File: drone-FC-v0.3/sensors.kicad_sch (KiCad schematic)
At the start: 34 parts, among them J2 Conn_01x04_Pin, J6 Conn_01x04_Pin, J7 ICM, J8 UART0, U3 LSM6DSOX, U4 MS5607-02BA, U5 LIS3MDL, U6 LIS3MDL, U7 MS5607-02BA, U8 LSM6DSOX, U9 BMI088

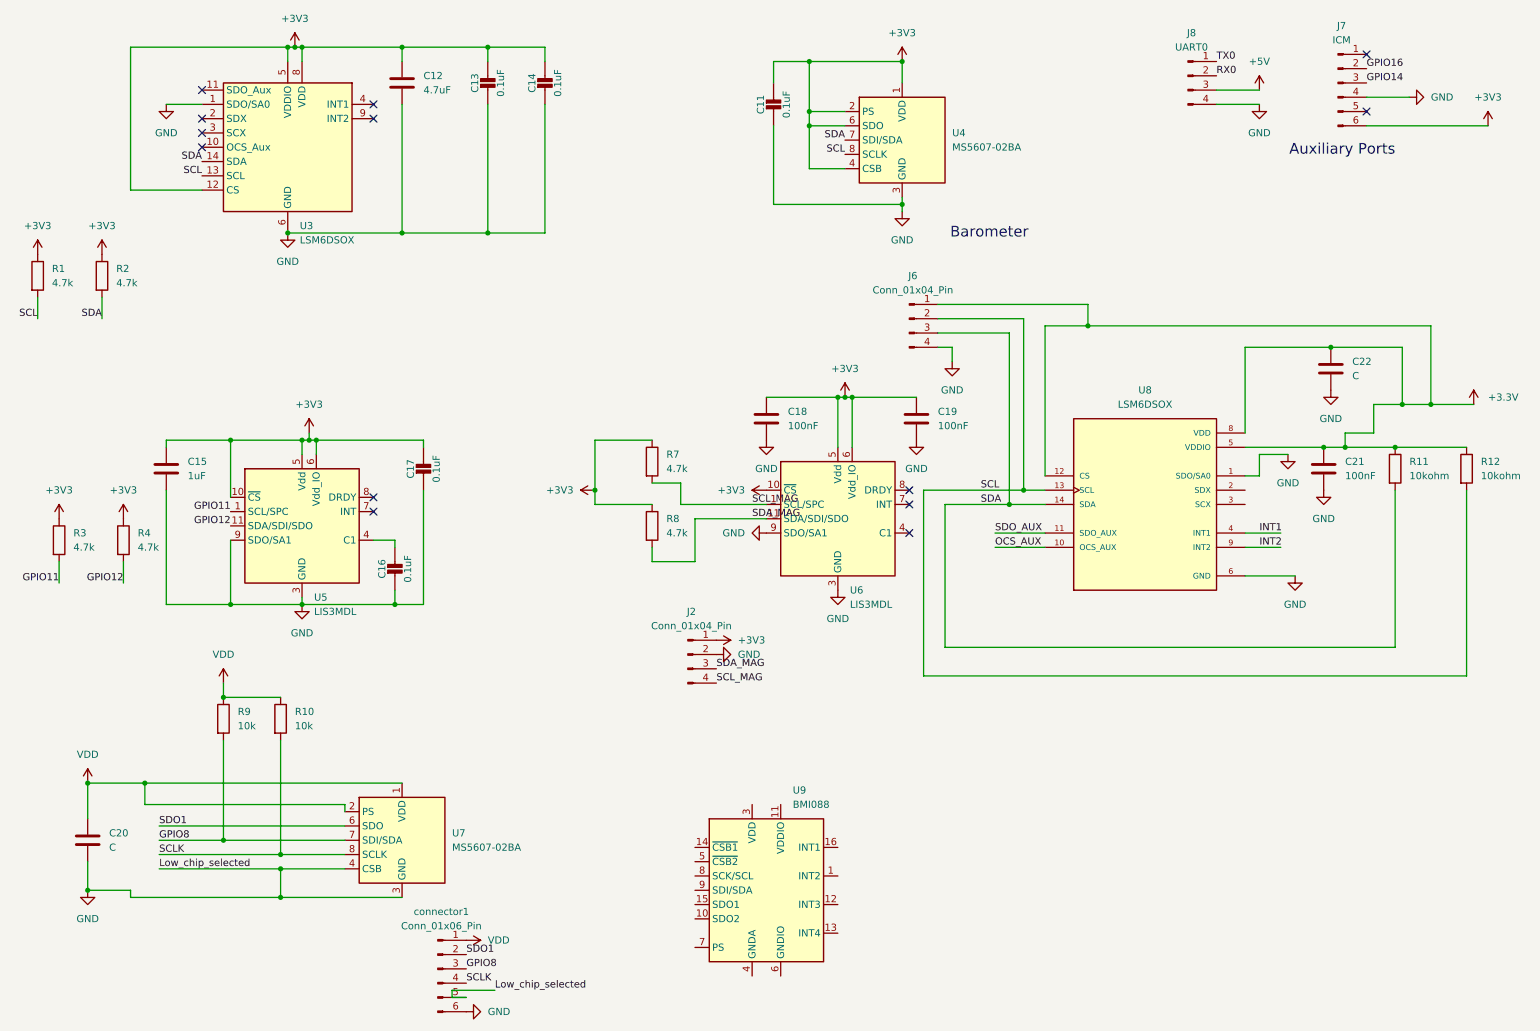
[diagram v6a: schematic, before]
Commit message: modified the schematics to three sensors and added some of the PCB layouts
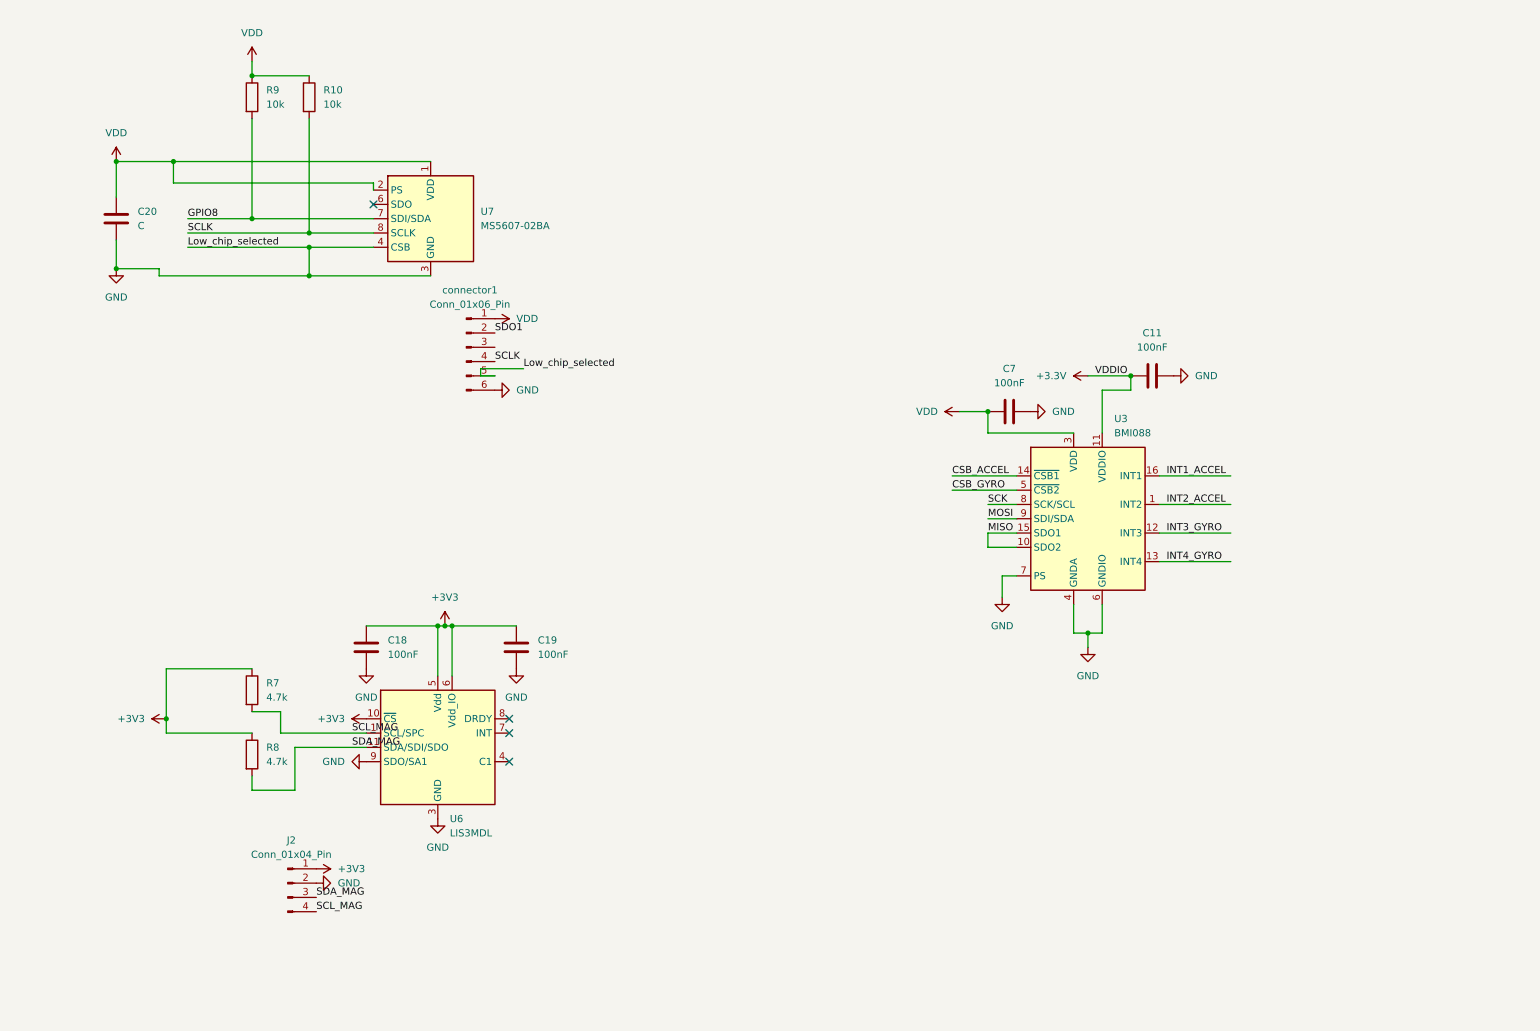
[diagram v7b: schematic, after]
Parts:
- removed C11, C13: 0.1uF, Capacitor_SMD:C_0603_1608Metric_Pad1.08x0.95mm_HandSolder, symbol ICM-eagle-import:CAP_CERAMIC0603_NO
- removed C12: 4.7uF, Capacitor_SMD:C_0603_1608Metric, symbol Device:C
- removed C14, C16, C17: 0.1uF, Capacitor_SMD:C_0603_1608Metric, symbol ICM-eagle-import:CAP_CERAMIC0603_NO
- removed C15: 1uF, Capacitor_SMD:C_0603_1608Metric, symbol Device:C
- removed C21: 100nF, Capacitor_SMD:C_0603_1608Metric_Pad1.08x0.95mm_HandSolder, symbol Device:C
- removed C22: C, Capacitor_SMD:C_0603_1608Metric_Pad1.08x0.95mm_HandSolder, symbol Device:C
- removed J6: Conn_01x04_Pin, Connector_PinSocket_2.00mm:PinSocket_1x04_P2.00mm_Vertical, symbol Connector:Conn_01x04_Pin
- removed J7: ICM, Connector_PinHeader_2.54mm:PinHeader_1x06_P2.54mm_Vertical, symbol Connector:Conn_01x06_Pin
- removed J8: UART0, Connector_PinHeader_2.54mm:PinHeader_1x04_P2.54mm_Vertical, symbol Connector:Conn_01x04_Pin
- removed R1, R2, R3, R4: 4.7k, Resistor_SMD:R_0603_1608Metric, symbol Device:R
- removed R11, R12: 10kohm, Resistor_SMD:R_0603_1608Metric_Pad0.98x0.95mm_HandSolder, symbol Device:R
- removed U3: LSM6DSOX, Package_LGA:LGA-14_3x2.5mm_P0.5mm_LayoutBorder3x4y, symbol Sensor_Motion:LSM6DSM
- removed U4: MS5607-02BA, Package_LGA:LGA-8_3x5mm_P1.25mm, symbol Sensor_Pressure:MS5607-02BA
- removed U5: LIS3MDL, Package_LGA:LGA-12_2x2mm_P0.5mm, symbol Sensor_Magnetic:LIS3MDL
- removed U8: LSM6DSOX, Package_LGA:LGA-14_3x2.5mm_P0.5mm_LayoutBorder3x4y, symbol LSM6DSOX:LSM6DSOX
- removed U9: BMI088, Package_LGA:Bosch_LGA-16_4.5x3mm_P0.5mm_LayoutBorder7x1y_ClockwisePinNumbering, symbol Sensor_Motion:BMI088
- added C11, C7: 100nF, Capacitor_SMD:C_0603_1608Metric, symbol Device:C
- added U3: BMI088, Package_LGA:Bosch_LGA-16_4.5x3mm_P0.5mm_LayoutBorder7x1y_ClockwisePinNumbering, symbol Sensor_Motion:BMI088
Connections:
- net +3.3V: now also C11.1, U3.11 (VDDIO)
- net GND: now also C11.2, C7.2, U3.2 (GNDA), U3.4 (GNDA), U3.6 (GNDIO), U3.7 (PS)
- net GPIO8: no longer connector1.3 (Pin_3)
- net SDO1: no longer U7.6 (SDO)
- net VDD: now also C7.1, U3.3 (VDD)
- new net CSB_ACCEL: U3.14 (~{CSB1})
- new net CSB_GYRO: U3.5 (~{CSB2})
- new net INT1_ACCEL: U3.16 (INT1)
- new net INT2_ACCEL: U3.1 (INT2)
- new net INT3_GYRO: U3.12 (INT3)
- new net INT4_GYRO: U3.13 (INT4)
- new net MISO: U3.10 (SDO2), U3.15 (SDO1)
- new net MOSI: U3.9 (SDI/SDA)
- new net SCK: U3.8 (SCK/SCL)
- no-connect marks 13 -> 4
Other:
- note removed: "Auxiliary Ports"
- note removed: "Barometer"
- moved on the sheet: C18, C19, C20, J2, R10, R7, R8, R9, U6, U7, connector1

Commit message: "global labels added"
"global labels added"
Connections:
- net GPIO8 renamed GPIO 8
